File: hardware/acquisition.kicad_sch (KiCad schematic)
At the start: 9 parts, among them J5 Conn_T7_I2C, U1 ADS1115IDGS (0x48), U2 ADS1115IDGS (0x49)

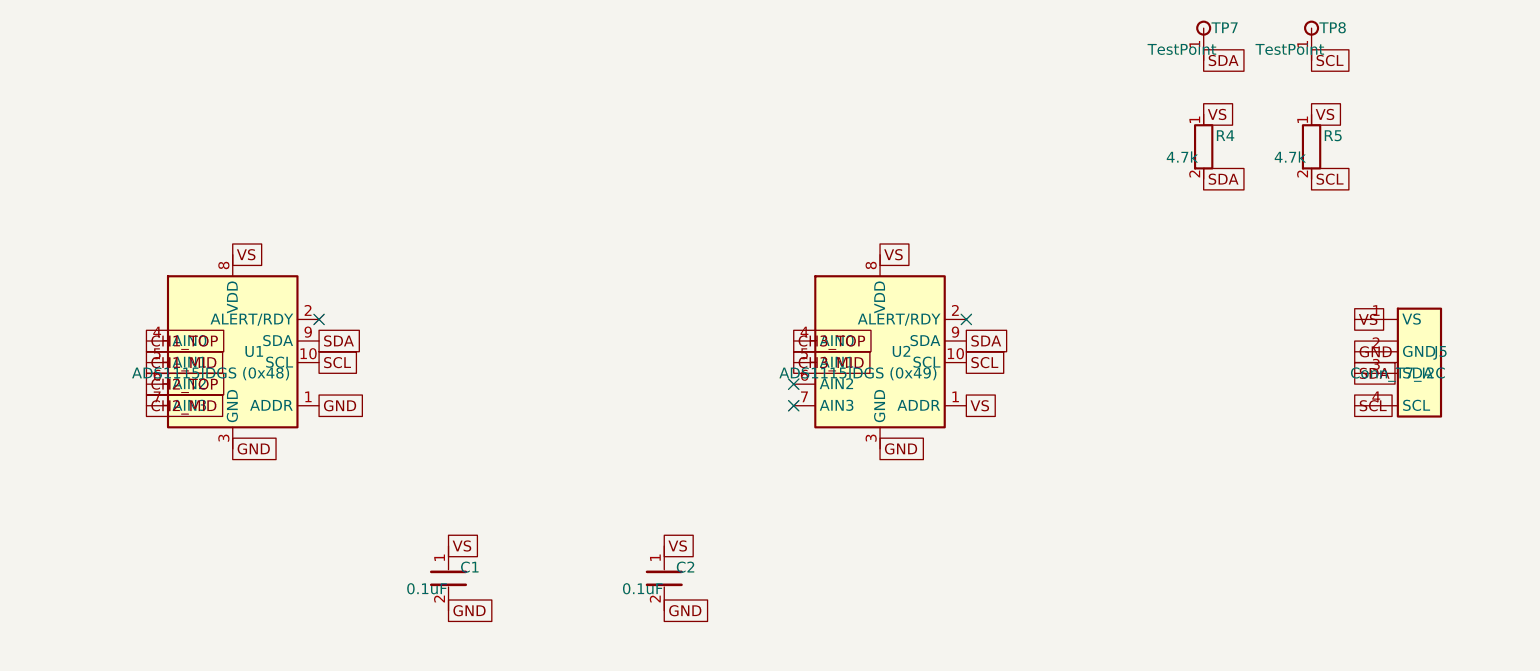
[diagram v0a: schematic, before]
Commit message: trackE: wire-up pass -- drawn wires + power symbols (netlist unchanged)
Convert the label-based capture to a conventionally drawn schematic: unit cells
as a drawn series current-loop (+5V/GND power symbols, CRD->R_ref->RTD, tapped
TOP/MID to TPs+labels); acquisition/power_io pins stub to power symbols/labels;
cross-sheet signals stay labelled. Fixed a y-down rotation bug (CRD anode/cathode
swap) by rotating the CRD 90 not 270.

ERC 0 errors / 0 warnings. Netlist node-for-node IDENTICAL to the pre-wiring
verified netlist (21 nets, diff empty); sim/netlists refreshed.

Co-Authored-By: Claude Opus 4.8 <noreply@anthropic.com>
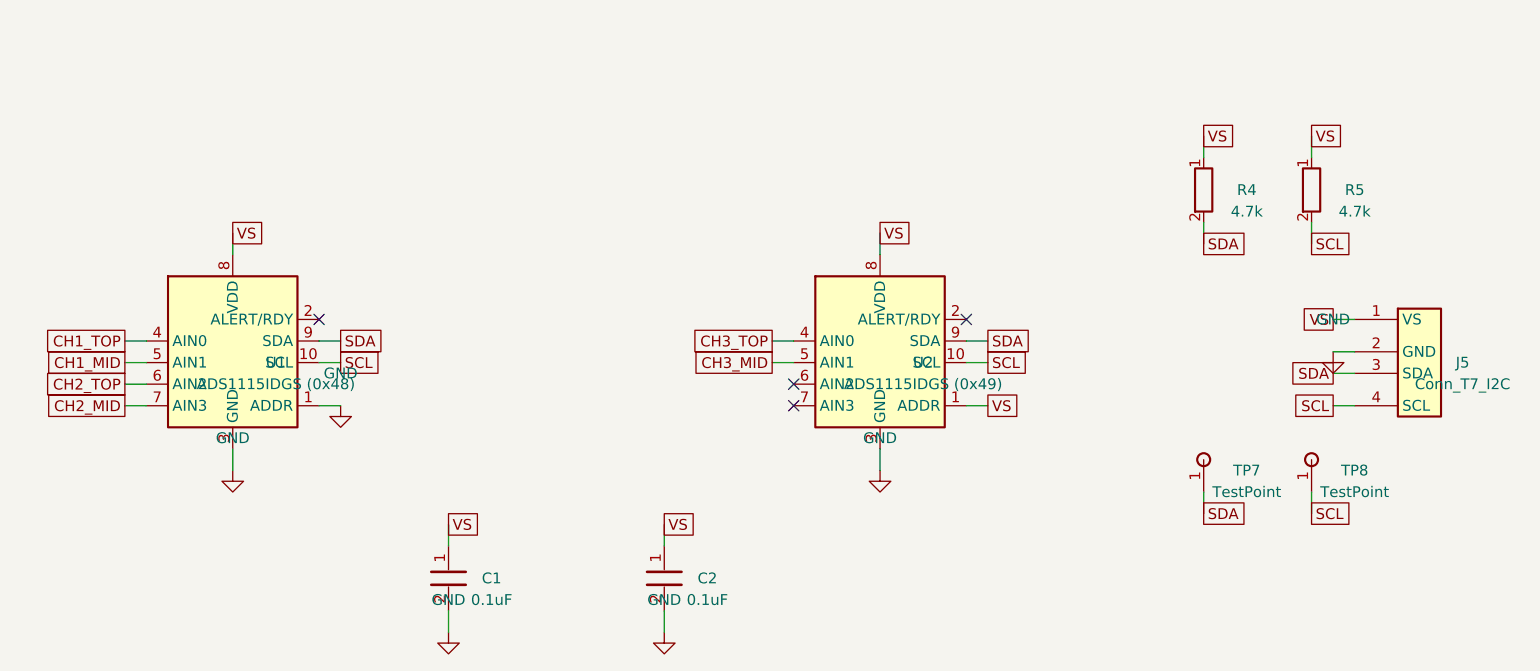
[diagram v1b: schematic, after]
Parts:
- removed U2: ADS1115IDGS (0x49), rtd-readout:MSOP-10_3x3mm_P0.5mm, symbol rtd-readout:ADS1115
- added TP7: TestPoint, rtd-readout:TestPoint_Pad_D1.5mm, symbol rtd-readout:TestPoint
- U2: renamed from TP7; value TestPoint -> ADS1115IDGS (0x49); footprint rtd-readout:TestPoint_Pad_D1.5mm -> rtd-readout:MSOP-10_3x3mm_P0.5mm; symbol rtd-readout:TestPoint -> rtd-readout:ADS1115; I2C_Address (none) -> ADDR strap -> address: GND=0x48, VDD=0x49, SDA=0x4A, SCL=0x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; MPN (copper pad) -> ADS1115IDGSR; Manufacturer (n/a) -> Texas Instruments; Package (none) -> VSSOP-10 / DGS (JEDEC MO-187 var BA, 3x3 mm, 0.5 mm pitch)
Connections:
- net CH3_MID: now also U2.5 (AIN1)
- net CH3_TOP: now also U2.4 (AIN0)
- net GND: now also U2.3 (GND)
- net SCL: now also U2.10 (SCL)
- net SDA: now also U2.9 (SDA), TP7.1; no longer U2.1
- net VS: now also U2.1 (ADDR), U2.8 (VDD)

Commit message: rev-B: real Digi-Key parts + layout review (copper unchanged)
Independent layout review + adversarial verify: 4-layer split planes, single-
point analog/digital GND tie, Kelvin intact -> fabricable (yes-with-fixes).
Real Digi-Key MPNs on the whole BOM; fixed RTD conn P/N (1729160 6-pos ->
1729144 4-pos) and R_ref tempco (25ppm -> Vishay TNPU1206 <=10ppm per spec).
ERC 0/0, DRC 0/0. Open decision: sense-line RC filter (see USER_MANUAL 8.5).

Co-Authored-By: Claude Opus 4.8 <noreply@anthropic.com>
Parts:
- C1, C2: MPN (set per value at BOM time) -> GRM188R71H104KA93D; Manufacturer (generic) -> Murata
- J5: MPN (1x4 2.54 mm header) -> PREC004SAAN-RC; Manufacturer (generic) -> Sullins
- R4, R5: MPN (set per value at BOM time) -> RC0805FR-074K7L; Manufacturer (generic) -> Yageo
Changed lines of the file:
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@@
 			)
 		)
-		(property "MPN" "(set per value at BOM time)"
+		(property "MPN" "GRM188R71H104KA93D"
 			(at 101.6 101.6 0)
 			(show_name no)
@@
 			)
 		)
-		(property "Manufacturer" "(generic)"
+		(property "Manufacturer" "Murata"
 			(at 101.6 101.6 0)
 			(show_name no)
@@
 			)
 		)
-		(property "MPN" "(set per value at BOM time)"
-			(at 127 101.6 0)
-			(show_name no)
-			(do_not_autoplace no)
-			(hide yes)
-			(effects
-				(font
-					(size 1.27 1.27)
-				)
-			)
-		)
-		(property "Manufacturer" "(generic)"
+		(property "MPN" "GRM188R71H104KA93D"
+			(at 127 101.6 0)
+			(show_name no)
+			(do_not_autoplace no)
+			(hide yes)
+			(effects
+				(font
+					(size 1.27 1.27)
+				)
+			)
+		)
+		(property "Manufacturer" "Murata"
 			(at 127 101.6 0)
 			(show_name no)
@@
 			)
 		)
-		(property "MPN" "(set per value at BOM time)"
-			(at 190.5 55.88 0)
-			(show_name no)
-			(do_not_autoplace no)
-			(hide yes)
-			(effects
-				(font
-					(size 1.27 1.27)
-				)
-			)
-		)
-		(property "Manufacturer" "(generic)"
+		(property "MPN" "RC0805FR-074K7L"
+			(at 190.5 55.88 0)
+			(show_name no)
+			(do_not_autoplace no)
+			(hide yes)
+			(effects
+				(font
+					(size 1.27 1.27)
+				)
+			)
+		)
+		(property "Manufacturer" "Yageo"
 			(at 190.5 55.88 0)
 			(show_name no)
@@
 			)
 		)
-		(property "MPN" "(set per value at BOM time)"
-			(at 203.2 55.88 0)
-			(show_name no)
-			(do_not_autoplace no)
-			(hide yes)
-			(effects
-				(font
-					(size 1.27 1.27)
-				)
-			)
-		)
-		(property "Manufacturer" "(generic)"
+		(property "MPN" "RC0805FR-074K7L"
+			(at 203.2 55.88 0)
+			(show_name no)
+			(do_not_autoplace no)
+			(hide yes)
+			(effects
+				(font
+					(size 1.27 1.27)
+				)
+			)
+		)
+		(property "Manufacturer" "Yageo"
 			(at 203.2 55.88 0)
 			(show_name no)
@@
 			)
 		)
-		(property "MPN" "(1x4 2.54 mm header)"
+		(property "MPN" "PREC004SAAN-RC"
 			(at 215.9 76.2 0)
 			(show_name no)
@@
 			)
 		)
-		(property "Manufacturer" "(generic)"
+		(property "Manufacturer" "Sullins"
 			(at 215.9 76.2 0)
 			(show_name no)
